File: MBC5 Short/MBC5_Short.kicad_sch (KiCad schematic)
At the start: 0 parts

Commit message: Add MBC5 chips (ROM, FRAM, MBC5) to schematic, not wired yet
A few of the symbols came from HDR's https://github.com/HDR/Game-Boy-KiCad-Library, thank you thank you!!
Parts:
- added U1: MBM29F033C, Package_SO:TSOP-I-40_18.4x10mm_P0.5mm, symbol mbm29f033c:MBM29F033C
- added U2: MBC5, Package_QFP:LQFP-32_7x7mm_P0.8mm, symbol Gameboy:MBC5
- added U3: FM18W08, Package_SO:SOIC-28W_7.5x17.9mm_P1.27mm, symbol Memory_NVRAM:FM18W08-SG
- added U99: CartBus, Connector_GameBoy:GameBoy_GamePak_AGB-002_P1.50mm_Edge, symbol Gameboy:CartBus
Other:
- note added: "CartBus"
- note added: "FRAM Circuit"
- note added: "MBC5 Circuit"
- note added: "ROM Circuit"

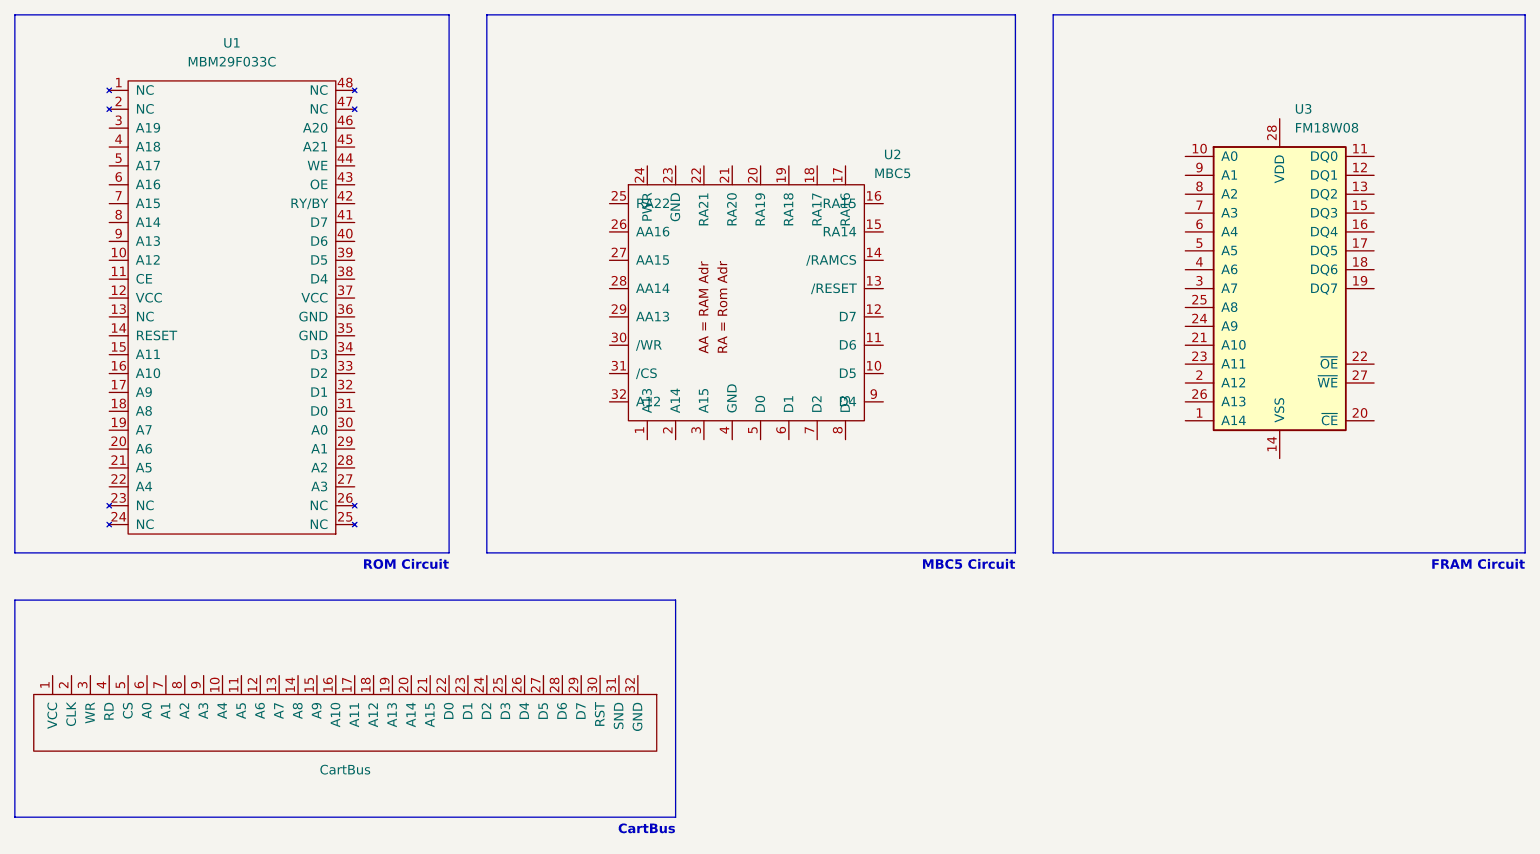
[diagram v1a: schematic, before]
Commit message: Add little jumper wires off each connection for ease
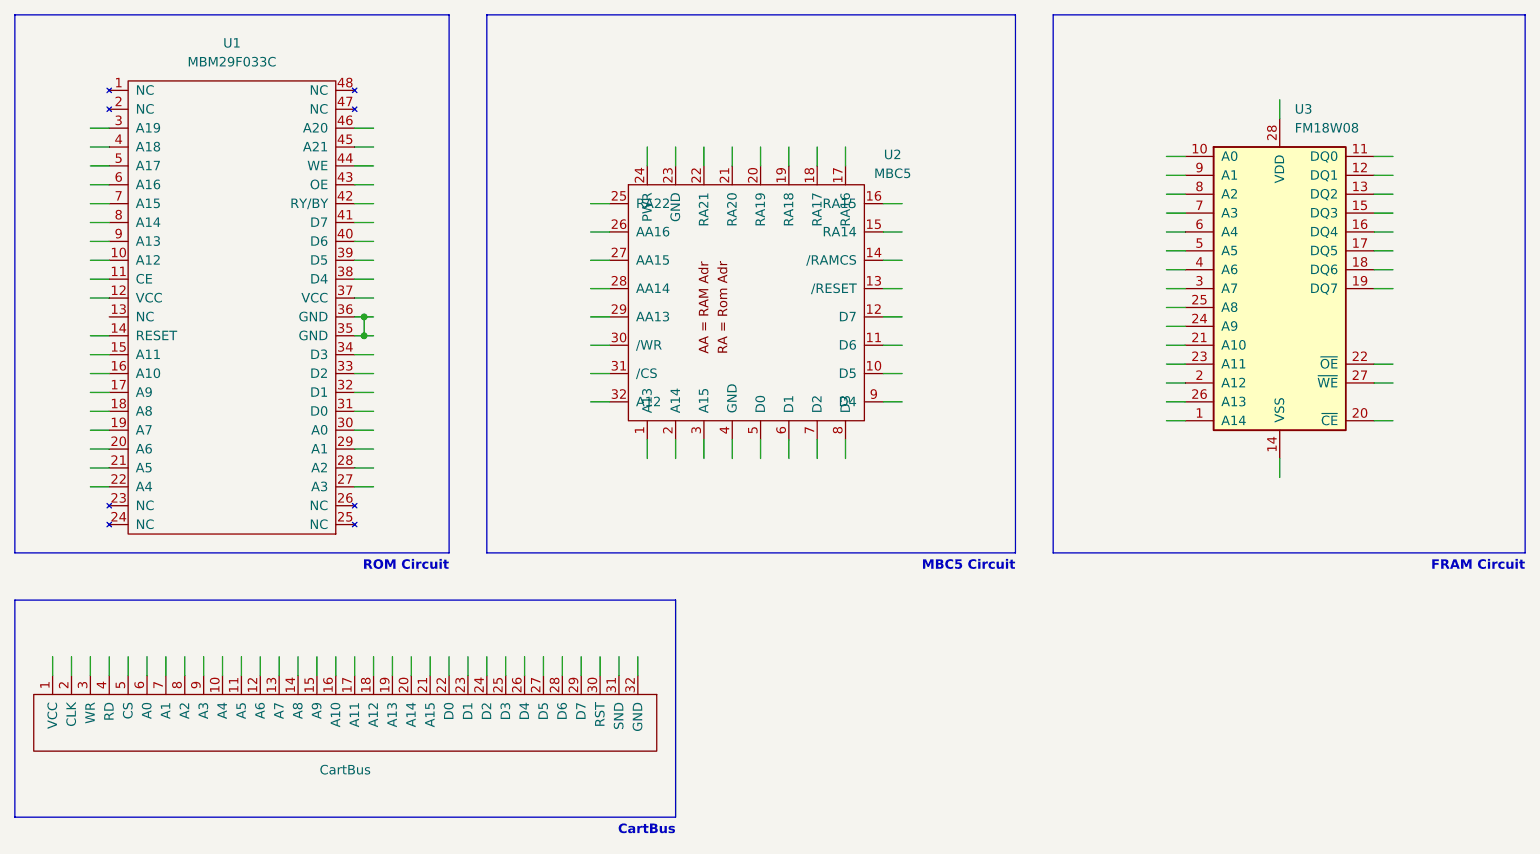
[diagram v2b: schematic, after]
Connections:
- net at U1.35 (GND): now also U1.36 (GND)

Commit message: Add nets between all components
This generally, again, follows the work from HDR via https://github.com/HDR/MBC5-Flashcart/blob/29cbd084a0546ef0b45e91f31f956e2d148b7e93/MBC5%20Flashcart%20Schematic.pdf but I did try to corroborate it with other sources too.
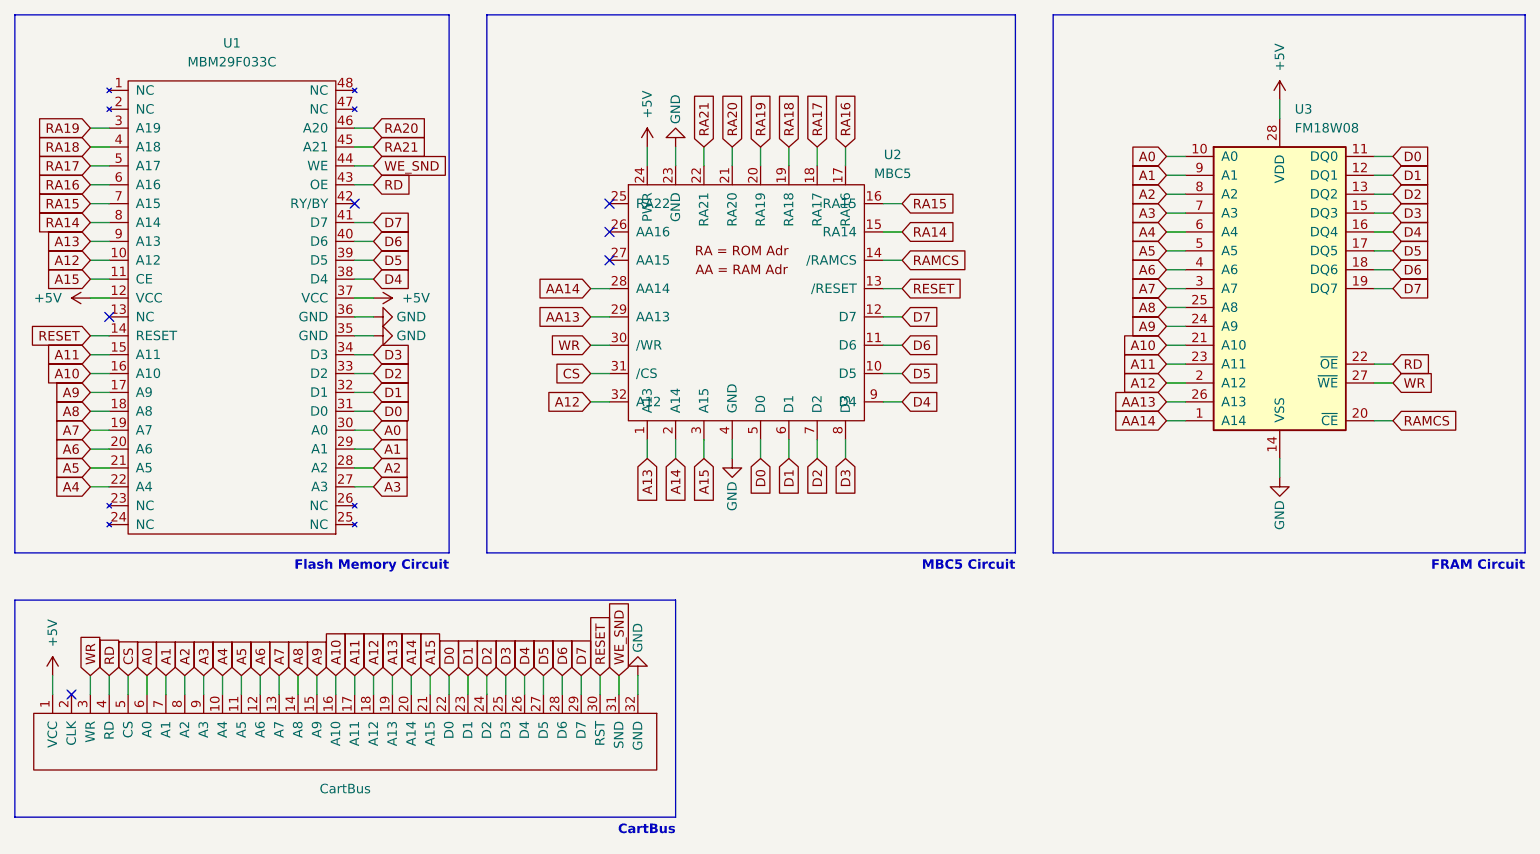
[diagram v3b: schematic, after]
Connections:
- net A12: now reaches U1.10 (A12)
- net A12: now also U2.32 (A12), U3.2 (A12), U99.18 (A12)
- net A15: now reaches U1.11 (CE)
- net A15: now also U2.3 (A15), U99.21 (A15)
- net +5V: now reaches U1.12 (VCC)
- net +5V: now also U1.37 (VCC), U2.24 (PWR), U3.28 (VDD), U99.1 (VCC)
- net RESET: now reaches U1.14 (RESET)
- net RESET: now also U2.13 (/RESET), U99.30 (RST)
- net A11: now reaches U1.15 (A11)
- net A11: now also U3.23 (A11), U99.17 (A11)
- net A10: now reaches U1.16 (A10)
- net A10: now also U3.21 (A10), U99.16 (A10)
- net A9: now reaches U1.17 (A9)
- net A9: now also U3.24 (A9), U99.15 (A9)
- net A8: now reaches U1.18 (A8)
- net A8: now also U3.25 (A8), U99.14 (A8)
- net A7: now reaches U1.19 (A7)
- net A7: now also U3.3 (A7), U99.13 (A7)
- net A6: now reaches U1.20 (A6)
- net A6: now also U3.4 (A6), U99.12 (A6)
- net A5: now reaches U1.21 (A5)
- net A5: now also U3.5 (A5), U99.11 (A5)
- net A4: now reaches U1.22 (A4)
- net A4: now also U3.6 (A4), U99.10 (A4)
- net A3: now reaches U1.27 (A3)
- net A3: now also U3.7 (A3), U99.9 (A3)
- net A2: now reaches U1.28 (A2)
- net A2: now also U3.8 (A2), U99.8 (A2)
- net A1: now reaches U1.29 (A1)
- net A1: now also U3.9 (A1), U99.7 (A1)
- net RA19: now reaches U1.3 (A19)
- net RA19: now also U2.20 (RA19)
- net A0: now reaches U1.30 (A0)
- net A0: now also U3.10 (A0), U99.6 (A0)
- net D0: now reaches U1.31 (D0)
- net D0: now also U2.5 (D0), U3.11 (DQ0), U99.22 (D0)
- net D1: now reaches U1.32 (D1)
- net D1: now also U2.6 (D1), U3.12 (DQ1), U99.23 (D1)
- net D2: now reaches U1.33 (D2)
- net D2: now also U2.7 (D2), U3.13 (DQ2), U99.24 (D2)
- net D3: now reaches U1.34 (D3)
- net D3: now also U2.8 (D3), U3.15 (DQ3), U99.25 (D3)
- net GND: now reaches U1.35 (GND), U1.36 (GND)
- net GND: now also U2.23 (GND), U2.4 (GND), U3.14 (VSS), U99.32 (GND)
- net D4: now reaches U1.38 (D4)
- net D4: now also U2.9 (D4), U3.16 (DQ4), U99.26 (D4)
- net D5: now reaches U1.39 (D5)
- net D5: now also U2.10 (D5), U3.17 (DQ5), U99.27 (D5)
- net RA18: now reaches U1.4 (A18)
- net RA18: now also U2.19 (RA18)
- net D6: now reaches U1.40 (D6)
- net D6: now also U2.11 (D6), U3.18 (DQ6), U99.28 (D6)
- net D7: now reaches U1.41 (D7)
- net D7: now also U2.12 (D7), U3.19 (DQ7), U99.29 (D7)
- net RD: now reaches U1.43 (OE)
- net RD: now also U3.22 (~{OE}), U99.4 (RD)
- net WE_SND: now reaches U1.44 (WE)
- net WE_SND: now also U99.31 (SND)
- net RA21: now reaches U1.45 (A21)
- net RA21: now also U2.22 (RA21)
- net RA20: now reaches U1.46 (A20)
- net RA20: now also U2.21 (RA20)
- net RA17: now reaches U1.5 (A17)
- net RA17: now also U2.18 (RA17)
- net RA16: now reaches U1.6 (A16)
- net RA16: now also U2.17 (RA16)
- net RA15: now reaches U1.7 (A15)
- net RA15: now also U2.16 (RA15)
- net RA14: now reaches U1.8 (A14)
- net RA14: now also U2.15 (RA14)
- net A13: now reaches U1.9 (A13)
- net A13: now also U2.1 (A13), U99.19 (A13)
- net AA14: now reaches U3.1 (A14)
- net AA14: now also U2.28 (AA14)
- net RAMCS: now reaches U3.20 (~{CE})
- net RAMCS: now also U2.14 (/RAMCS)
- net AA13: now reaches U3.26 (A13)
- net AA13: now also U2.29 (AA13)
- net WR: now reaches U3.27 (~{WE})
- net WR: now also U2.30 (/WR), U99.3 (WR)
- net A14: now reaches U99.20 (A14)
- net A14: now also U2.2 (A14)
- net CS: now reaches U99.5 (CS)
- net CS: now also U2.31 (/CS)
- no-connect marks 0 -> 6
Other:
- note added: "Flash Memory Circuit"
- note removed: "ROM Circuit"
